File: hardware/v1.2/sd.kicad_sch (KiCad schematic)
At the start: 10 parts, among them U1 ECP5-CABGA256, U11 W25Q128JVS

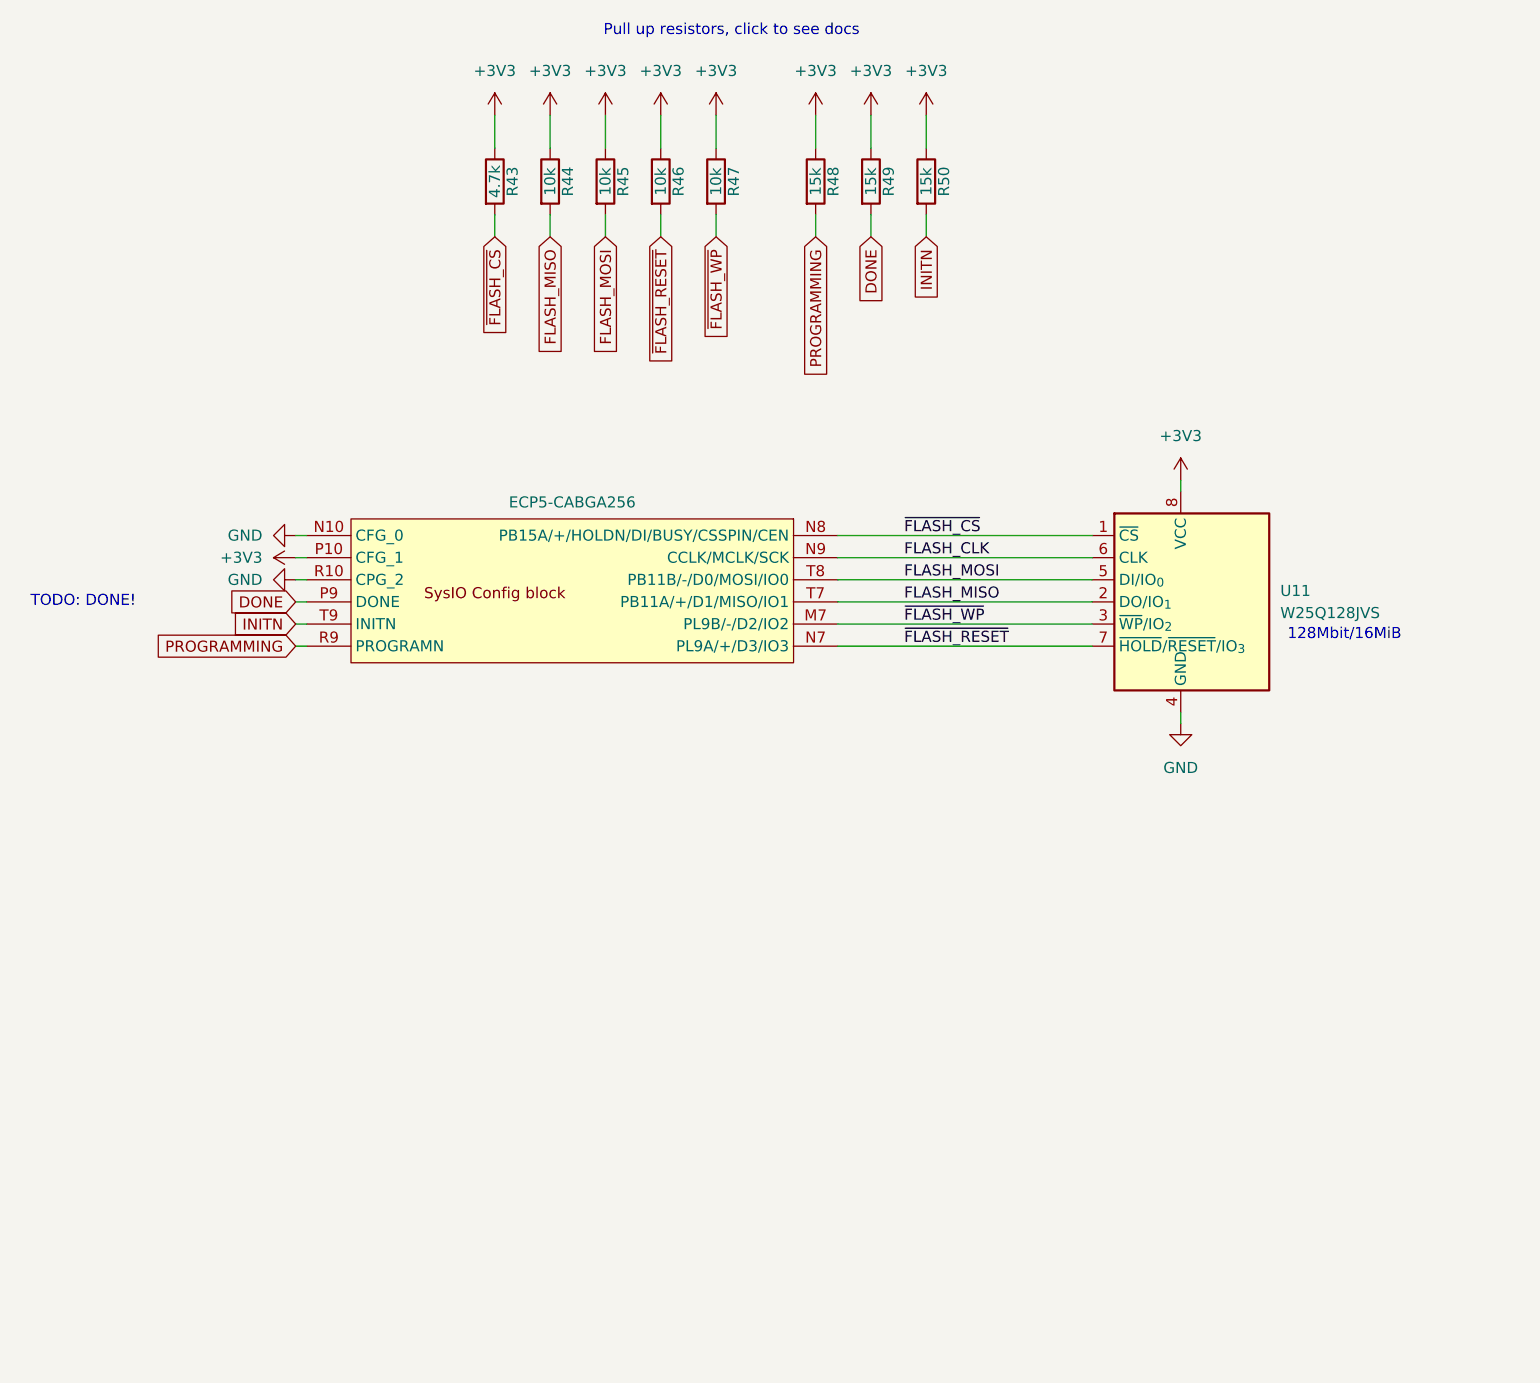
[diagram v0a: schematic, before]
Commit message: Custom ECP5-CABGA256 symbol
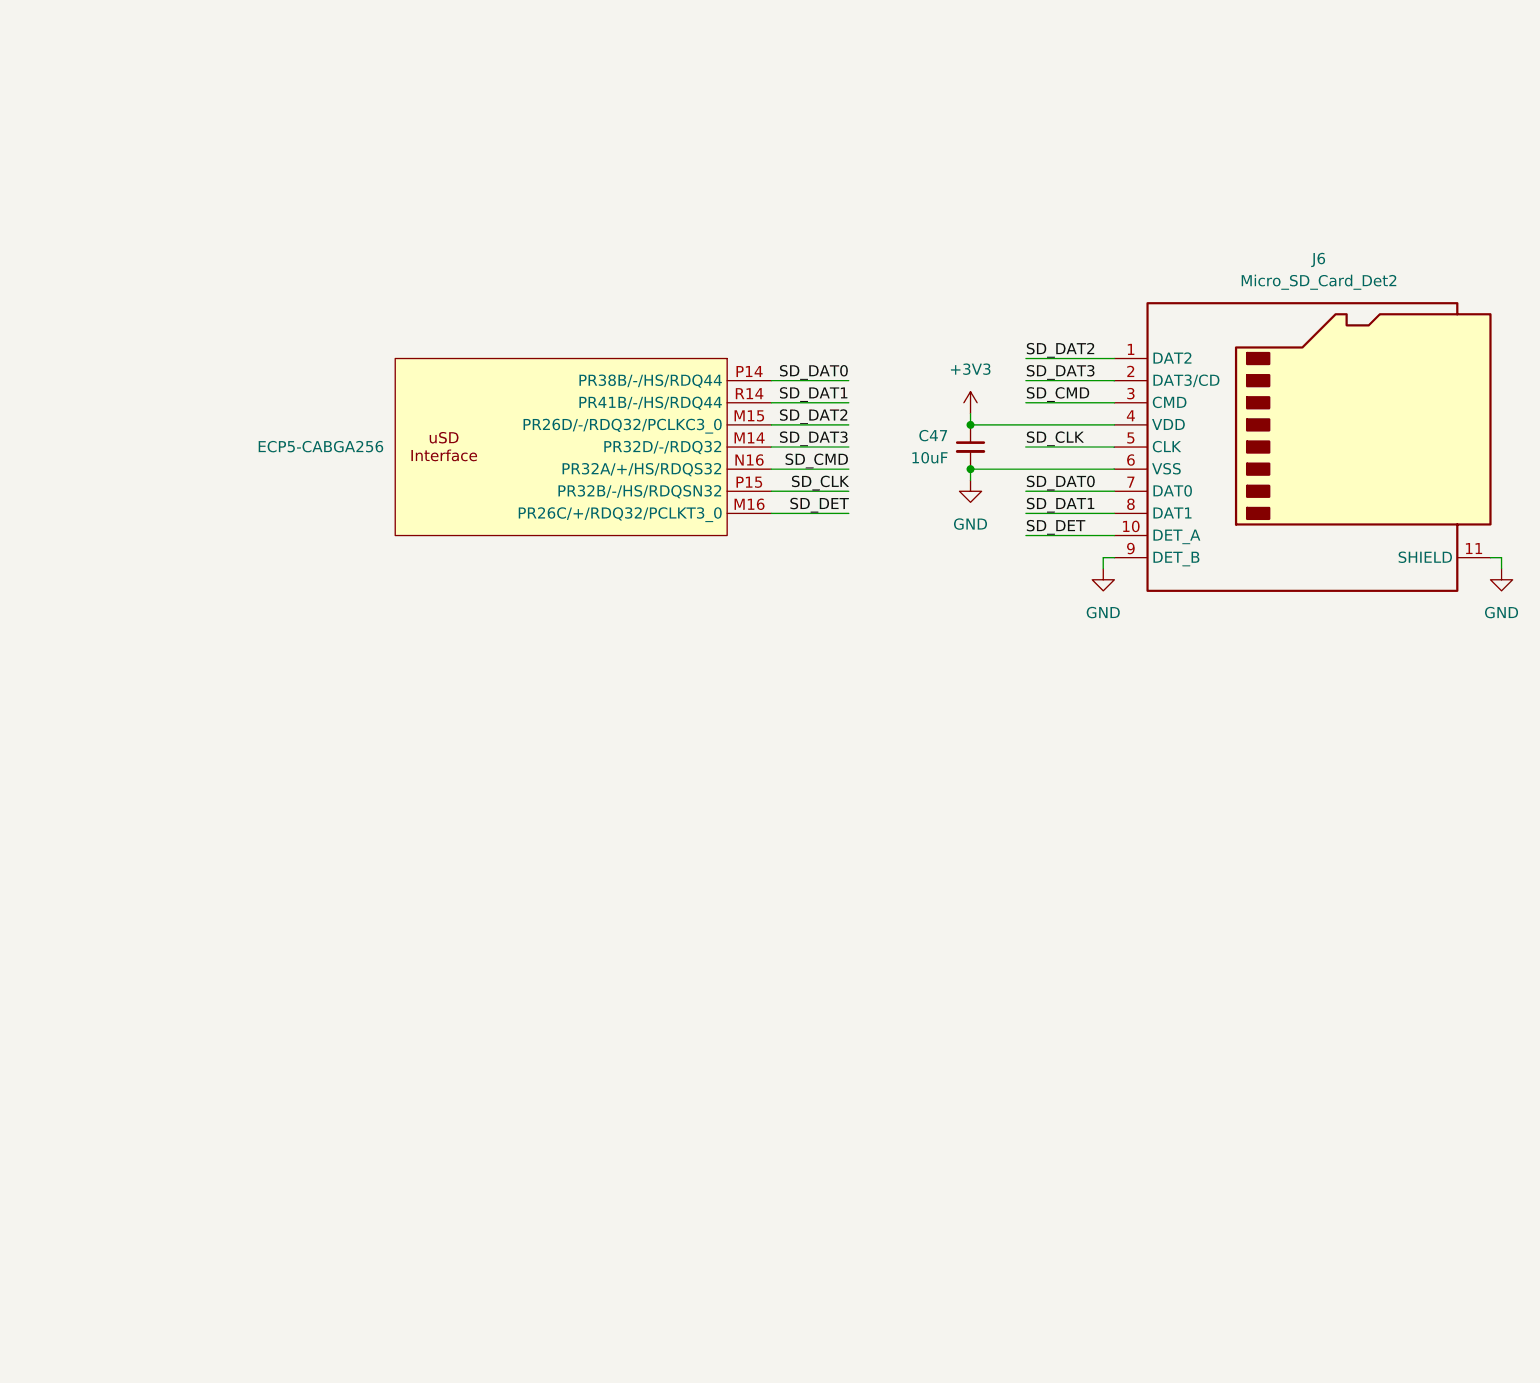
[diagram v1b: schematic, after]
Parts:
- removed R43: 4.7k, Resistor_SMD:R_0402_1005Metric, symbol Device:R
- removed R44, R45, R46, R47: 10k, Resistor_SMD:R_0402_1005Metric, symbol Device:R
- removed R48, R49, R50: 15k, Resistor_SMD:R_0402_1005Metric, symbol Device:R
- removed U1: ECP5-CABGA256, Package_BGA:BGA-256_14.0x14.0mm_Layout16x16_P0.8mm_Ball0.45mm_Pad0.32mm_NSMD, symbol icepi-lib:LFE5U-25F-6BG256x
- removed U11: W25Q128JVS, Package_SO:SOIC-8_5.3x5.3mm_P1.27mm, symbol Memory_Flash:W25Q128JVS
- added C47: 10uF, Capacitor_SMD:C_0603_1608Metric, symbol Device:C_Small
- added J6: Micro_SD_Card_Det2, icepi-lib:microSD_HC_SOFNG_TF-008, symbol Connector:Micro_SD_Card_Det2
- added U1: ECP5-CABGA256, Package_BGA:BGA-256_14.0x14.0mm_Layout16x16_P0.8mm_Ball0.45mm_Pad0.32mm_NSMD, symbol icepi-lib:LFE5U-25F-6BG256x
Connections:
- net +3V3: now also C47.1, J6.4 (VDD)
- net GND: now also C47.2, J6.11 (SHIELD), J6.6 (VSS), J6.9 (DET_B)
- new net SD_CLK: J6.5 (CLK), U1.P15 (PR32B/-/HS/RDQSN32)
- new net SD_CMD: J6.3 (CMD), U1.N16 (PR32A/+/HS/RDQS32)
- new net SD_DAT0: J6.7 (DAT0), U1.P14 (PR38B/-/HS/RDQ44)
- new net SD_DAT1: J6.8 (DAT1), U1.R14 (PR41B/-/HS/RDQ44)
- new net SD_DAT2: J6.1 (DAT2), U1.M15 (PR26D/-/RDQ32/PCLKC3_0)
- new net SD_DAT3: J6.2 (DAT3/CD), U1.M14 (PR32D/-/RDQ32)
- new net SD_DET: J6.10 (DET_A), U1.M16 (PR26C/+/RDQ32/PCLKT3_0)
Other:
- note removed: "128Mbit/16MiB"
- note removed: "Pull up resistors, click to see docs"
- note removed: "TODO: DONE!"

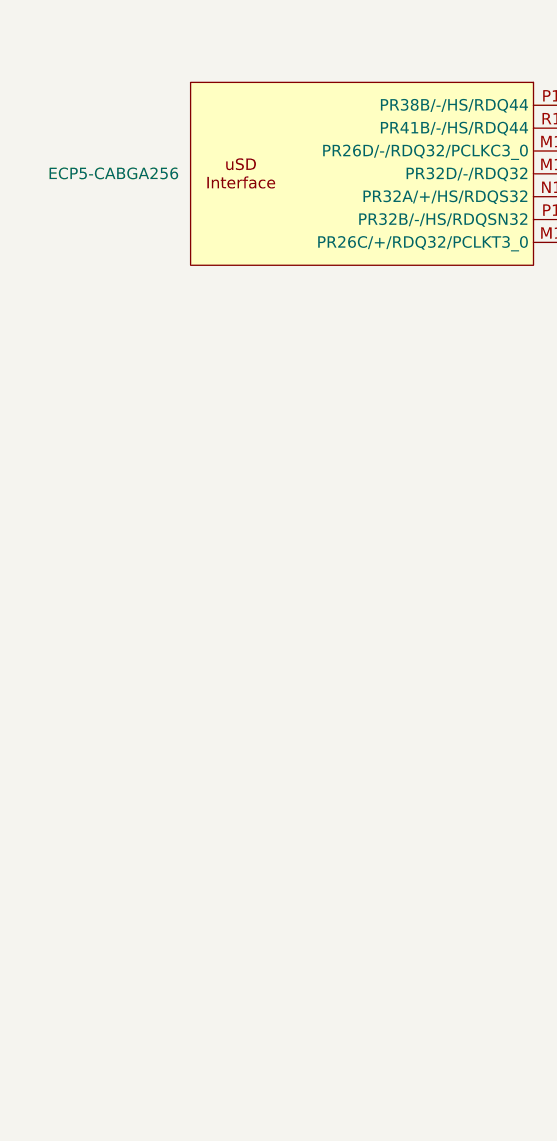
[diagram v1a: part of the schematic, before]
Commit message: UART to PS2 converter
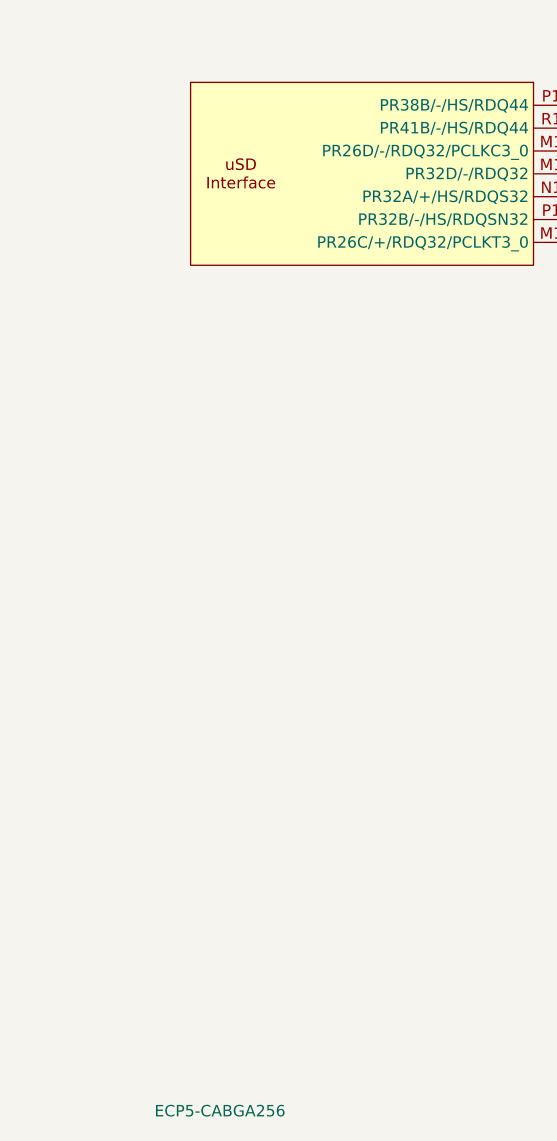
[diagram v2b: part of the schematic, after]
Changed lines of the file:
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@@
 		)
 		(property "Value" "ECP5-CABGA256"
-			(at 93.98 99.06 0)
+			(at 105.8067 203.2 0)
 			(effects
 				(font
@@
 		)
 		(instances
-			(project "icepi-zero"
+			(project ""
+				(path "/f88da08e-cf42-4d03-a08f-3f602fe6658d/17c9c9b3-f379-4e1f-a876-d3fcf0529a4d"
+					(reference "U1")
+					(unit 7)
+				)
 				(path "/f88da08e-cf42-4d03-a08f-3f602fe6658d/d38ad226-7226-4c8c-b808-74c724beb9de"
 					(reference "U1")
